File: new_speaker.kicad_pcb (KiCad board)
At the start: 2 copper layers, 45 x 53.5 mm, 11 parts, among them J1 Conn_01x02, J2 Conn_01x04_Pin, J3 Conn_01x03_Pin, U1 MAX98357A

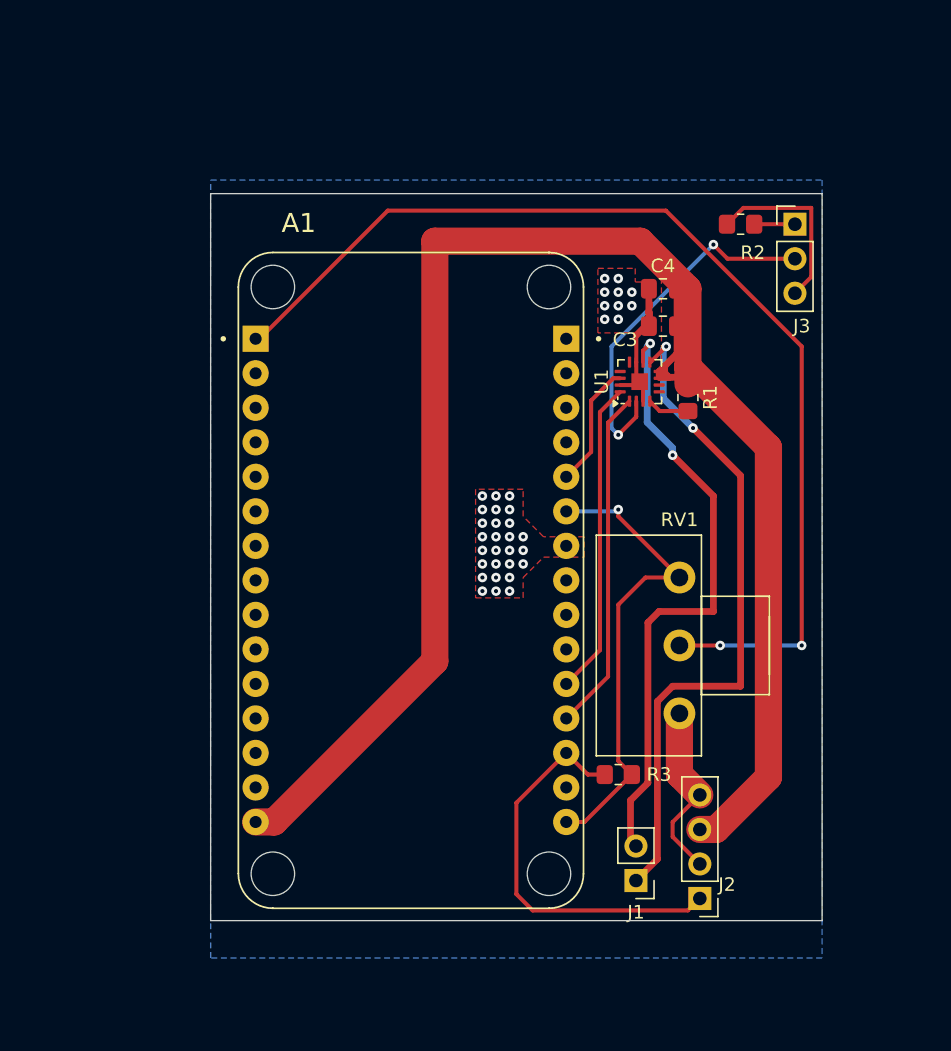
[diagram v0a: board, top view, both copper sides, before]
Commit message: fixed nodemcu footprint
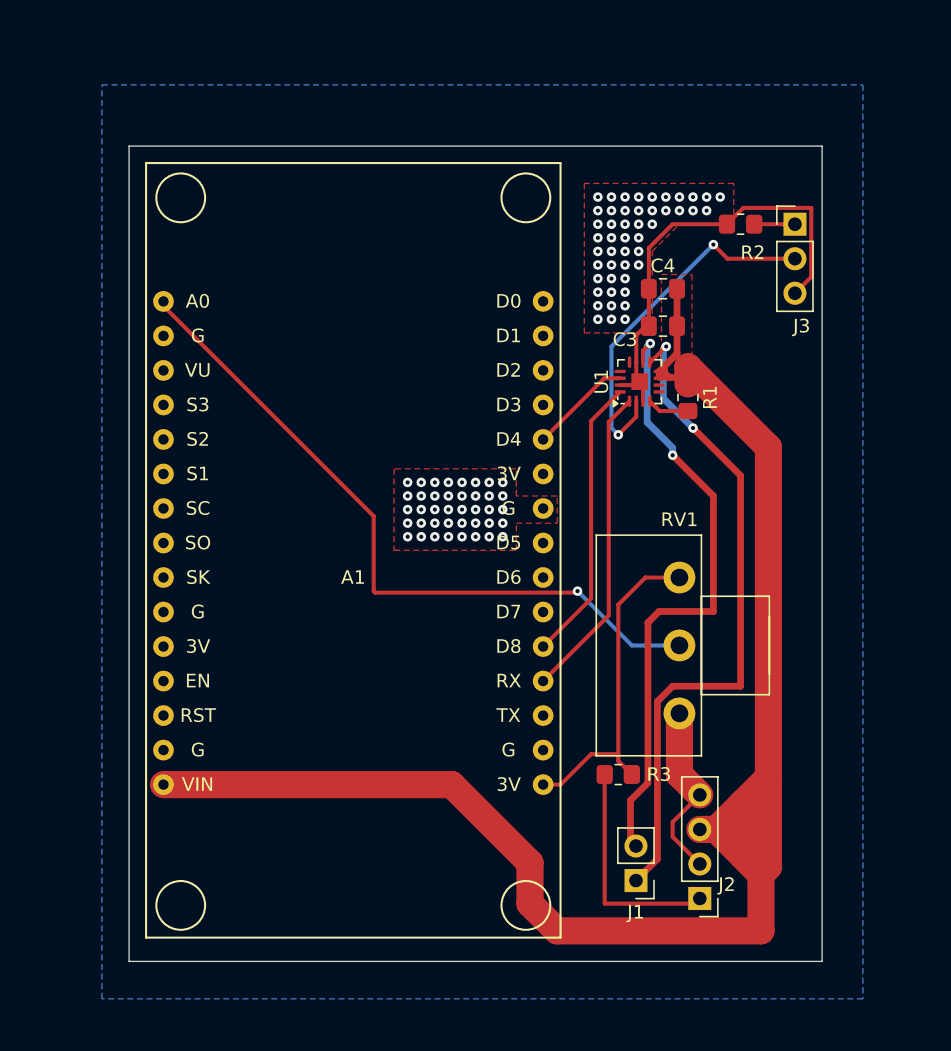
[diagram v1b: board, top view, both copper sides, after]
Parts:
- A1: value 113990105 -> ~; footprint footprints:SEEED_113990105 -> footprints:NodeMCU-LoLinV3
- moved A1 4.25 mm to (133.0, 97.0)
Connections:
- J2 pad 1: Net-(A1B-D10) -> Net-(J2-Pin_1)
- R3 pad 2: Net-(A1B-D10) -> Net-(J2-Pin_1)
- RV1 pad 2: Net-(A1A-A0) -> Net-(A1-A0)
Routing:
- net Net-(A1A-A0): track 79.2 -> 0.00 mm, vias 2 -> 0
- net Net-(A1-A0): track 0.00 -> 52.0 mm, vias 0 -> 1
- net Net-(A1B-D10): track 29.8 -> 0.00 mm
- net Net-(J2-Pin_1): track 0.00 -> 16.7 mm
- net +3.3V: track 35.3 -> 24.7 mm, vias 1 -> 0
- net GND: track 37.5 -> 46.9 mm, vias 37 -> 88
- net +5V: track 125.7 -> 123.0 mm
- net DIN: track 25.3 -> 23.2 mm
- net BCLK: track 23.1 -> 21.1 mm
- net LRC: track 9.19 -> 7.53 mm
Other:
- board size 45 x 53.5 mm -> 51 x 60 mm

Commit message: added mounting pads and rounded corners
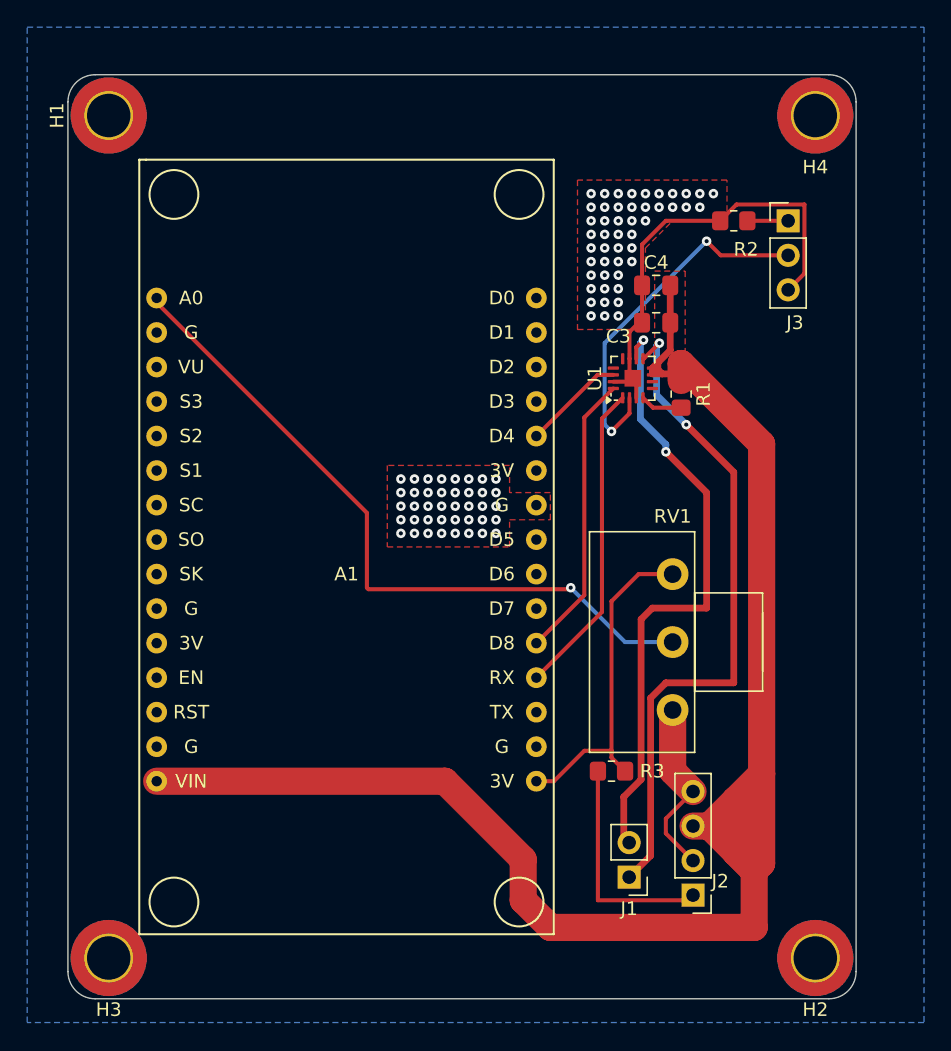
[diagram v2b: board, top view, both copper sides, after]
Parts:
- added H1: MountingHole_Pad, MountingHole:MountingHole_3.2mm_M3_DIN965_Pad_TopBottom, F.Cu at (115.0, 63.0)
- added H2: MountingHole_Pad, MountingHole:MountingHole_3.2mm_M3_DIN965_Pad_TopBottom, F.Cu at (167.0, 125.0)
- added H3: MountingHole_Pad, MountingHole:MountingHole_3.2mm_M3_DIN965_Pad_TopBottom, F.Cu at (115.0, 125.0)
- added H4: MountingHole_Pad, MountingHole:MountingHole_3.2mm_M3_DIN965_Pad_TopBottom, F.Cu at (167.0, 63.0)
- moved A1 0.56 mm to (132.5, 96.8)
- moved C3 0.56 mm to (155.3, 78.2)
- moved C4 0.56 mm to (155.3, 75.5)
- moved J1 0.56 mm to (153.3, 119.0)
- moved J2 0.56 mm to (158.0, 120.4)
- moved J3 0.56 mm to (165.0, 70.8)
- moved R1 0.56 mm to (157.1, 83.5)
- moved R2 0.56 mm to (161.0, 70.8)
- moved R3 0.56 mm to (152.0, 111.2)
- moved RV1 0.56 mm to (156.5, 106.8)
- moved U1 0.56 mm to (153.6, 82.3)
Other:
- board size 51 x 60 mm -> 58 x 68 mm

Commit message: fixed button input and added gain silkscreen
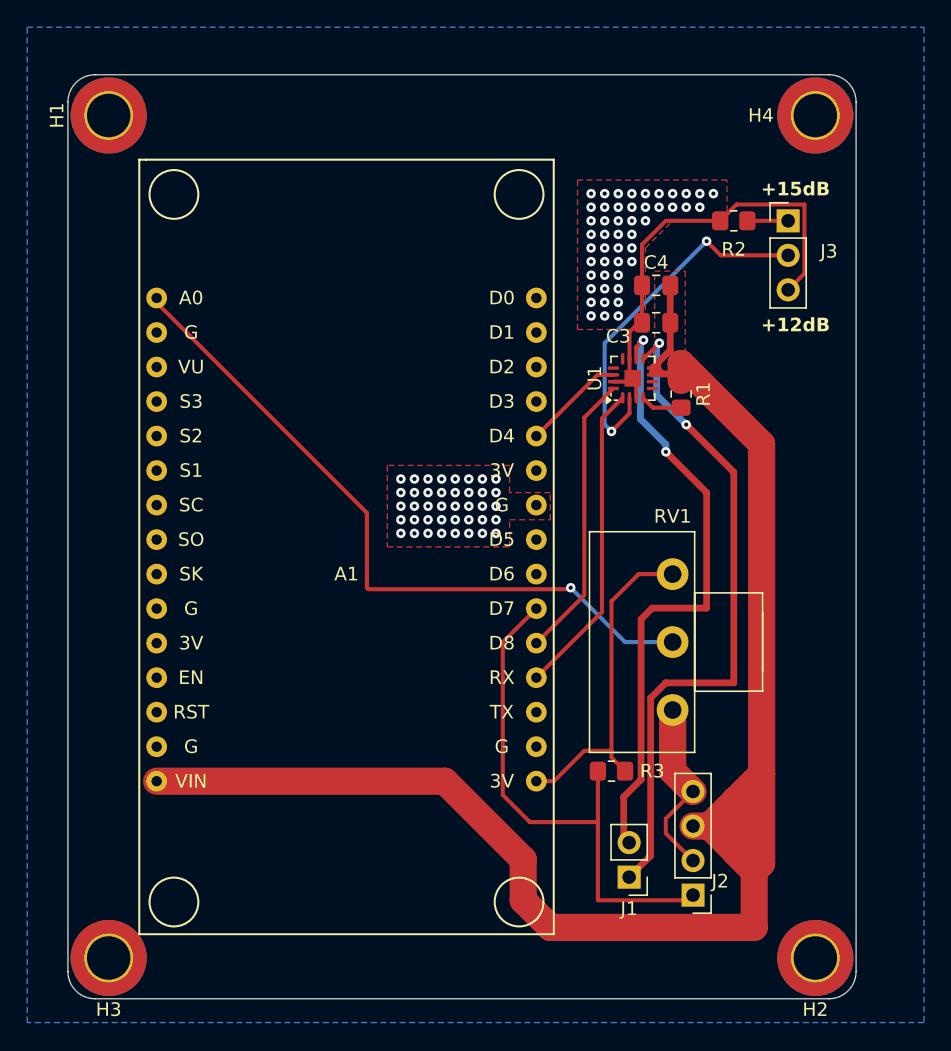
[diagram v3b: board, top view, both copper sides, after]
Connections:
- A1 pad 21: unconnected-(A1-D7-Pad21) -> Net-(A1-D7)
- J2 pad 1: Net-(J2-Pin_1) -> Net-(A1-D7)
- R3 pad 2: Net-(J2-Pin_1) -> Net-(A1-D7)
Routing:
- net Net-(A1-D7): track 0.00 -> 39.2 mm
- net Net-(J2-Pin_1): track 16.7 -> 0.00 mm
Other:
- board text added: "+12dB"
- board text added: "+15dB"
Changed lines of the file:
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@@
 	(net 14 "+5V")
 	(net 15 "Net-(J3-Pin_1)")
-	(net 16 "Net-(J2-Pin_1)")
+	(net 16 "Net-(A1-D7)")
 	(net 17 "Net-(A1-A0)")
 	(net 18 "unconnected-(A1-S0-Pad8)")
@@
 	(net 36 "unconnected-(A1-D6-Pad22)")
 	(net 37 "unconnected-(A1-D1-Pad29)")
-	(net 38 "unconnected-(A1-D7-Pad21)")
-	(net 39 "unconnected-(A1-3V-Pad25)")
-	(net 40 "unconnected-(A1-D2-Pad28)")
+	(net 38 "unconnected-(A1-3V-Pad25)")
+	(net 39 "unconnected-(A1-D2-Pad28)")
 	(footprint "Connector_PinHeader_2.54mm:PinHeader_1x03_P2.54mm_Vertical"
 		(layer "F.Cu")
@@
 		(tags "Through hole pin header THT 1x03 2.54mm single row")
 		(property "Reference" "J3"
-			(at 0.5 7.5 0)
+			(at 3 2.25 0)
 			(layer "F.SilkS")
 			(effects
@@
 			(layers "*.Cu" "*.Mask")
 			(remove_unused_layers no)
-			(net 16 "Net-(J2-Pin_1)")
+			(net 16 "Net-(A1-D7)")
 			(pinfunction "Pin_1")
 			(pintype "passive")
@@
 		(tags "mounting hole 3.2mm m3 din965")
 		(property "Reference" "H4"
-			(at 0 -3.8 180)
+			(at 4 0 180)
 			(layer "F.SilkS")
 			(effects
@@
 			(layers "*.Cu" "*.Mask" "F.SilkS")
 			(remove_unused_layers no)
-			(net 38 "unconnected-(A1-D7-Pad21)")
+			(net 16 "Net-(A1-D7)")
 			(pinfunction "D7")
-			(pintype "unspecified+no_connect")
+			(pintype "unspecified")
 		)
 		(pad "22" thru_hole circle
@@
 			(layers "*.Cu" "*.Mask" "F.SilkS")
 			(remove_unused_layers no)
-			(net 39 "unconnected-(A1-3V-Pad25)")
+			(net 38 "unconnected-(A1-3V-Pad25)")
 			(pinfunction "3V")
 			(pintype "power_out+no_connect")
@@
 			(layers "*.Cu" "*.Mask" "F.SilkS")
 			(remove_unused_layers no)
-			(net 40 "unconnected-(A1-D2-Pad28)")
+			(net 39 "unconnected-(A1-D2-Pad28)")
 			(pinfunction "D2")
 			(pintype "unspecified+no_connect")
@@
 			(layers "F.Cu" "F.Paste" "F.Mask")
 			(roundrect_rratio 0.208333)
-			(net 16 "Net-(J2-Pin_1)")
+			(net 16 "Net-(A1-D7)")
 			(pintype "passive")
 		)
@@
 		(tags "resistor handsolder")
 		(property "Reference" "R2"
-			(at 0.9 2.1 0)
+			(at 0 2.1 0)
 			(layer "F.SilkS")
 			(effects
@@
 		(layer "Edge.Cuts")
 	)
+	(gr_text "+12dB\n"
+		(at 163 79 0)
+		(layer "F.SilkS")
+		(effects
+			(font
+				(size 1 1)
+				(thickness 0.18)
+				(bold yes)
+			)
+			(justify left bottom)
+		)
+	)
+	(gr_text "+15dB\n"
+		(at 163 69 0)
+		(layer "F.SilkS")
+		(effects
+			(font
+				(size 1 1)
+				(thickness 0.18)
+				(bold yes)
+			)
+			(justify left bottom)
+		)
+	)
 	(segment
 		(start 152.1375 83.0875)
@@
 	)
 	(segment
-		(start 151 111.25)
+		(start 151 120.75)
+		(end 157.62 120.75)
+		(width 0.3)
+		(layer "F.Cu")
+		(net 16)
+	)
+	(segment
+		(start 151 115)
 		(end 151 120.75)
 		(width 0.3)
@@
 	)
 	(segment
-		(start 151 120.75)
-		(end 157.62 120.75)
+		(start 146 115)
+		(end 151 115)
+		(width 0.3)
+		(layer "F.Cu")
+		(net 16)
+	)
+	(segment
+		(start 144 101.76)
+		(end 144 113)
+		(width 0.3)
+		(layer "F.Cu")
+		(net 16)
+	)
+	(segment
+		(start 151 111.25)
+		(end 151 115)
+		(width 0.3)
+		(layer "F.Cu")
+		(net 16)
+	)
+	(segment
+		(start 146.47 99.29)
+		(end 144 101.76)
+		(width 0.3)
+		(layer "F.Cu")
+		(net 16)
+	)
+	(segment
+		(start 144 113)
+		(end 146 115)
 		(width 0.3)
 		(layer "F.Cu")
